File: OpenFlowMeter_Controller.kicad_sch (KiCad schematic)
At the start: 31 parts, among them J3 Conn_01x06, J5 Conn_01x03, J6 Conn_02x04_Odd_Even, J7 Conn_02x03_Odd_Even, U2 STM32F103C8Tx, U5 SN65HVD231, U7 24LC64, Y1 12 MHz

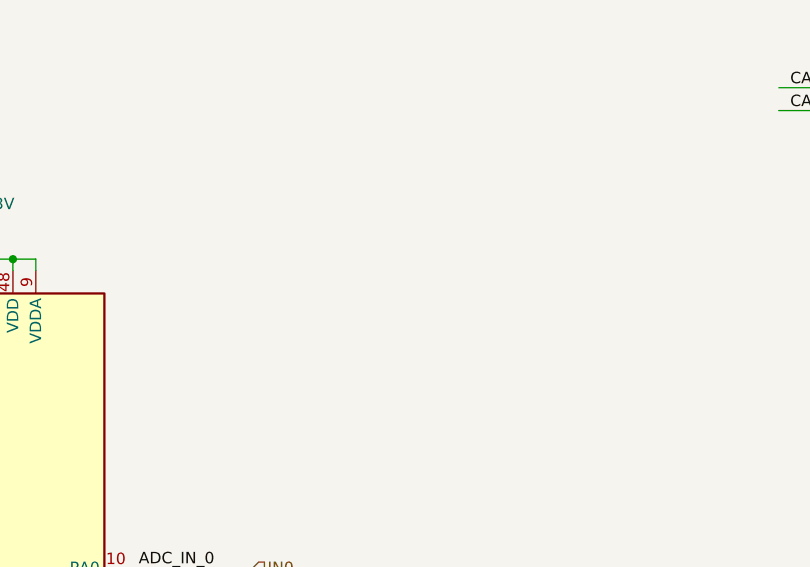
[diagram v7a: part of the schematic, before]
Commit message: added ADC protection
added Zener diodes as ADC input protection in combination with current limiting resistors.
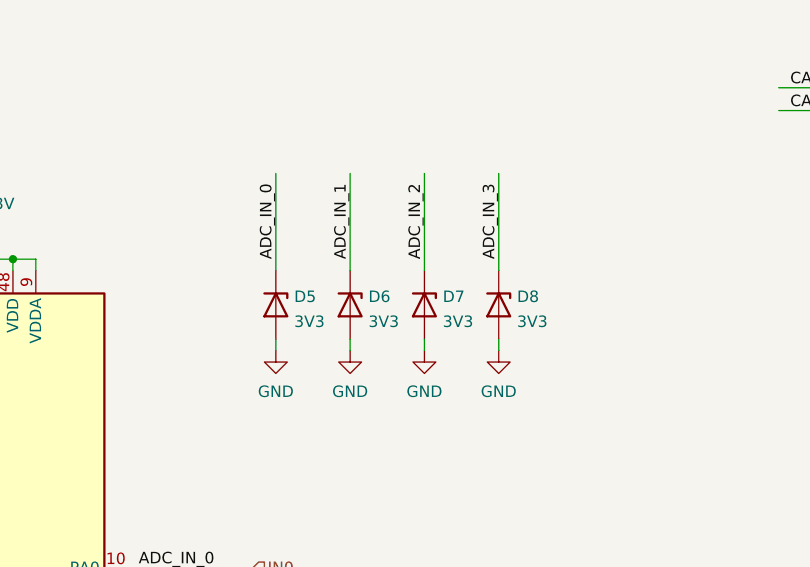
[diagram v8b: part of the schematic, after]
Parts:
- added D5, D6, D7, D8: 3V3, Diode_SMD:D_MiniMELF, symbol Device:D_Zener
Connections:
- net GND: now also D5.2 (A), D6.2 (A), D7.2 (A), D8.2 (A)
- net IN0: now also D5.1 (K)
- net IN1: now also D6.1 (K)
- net IN2: now also D7.1 (K)
- net IN3: now also D8.1 (K)
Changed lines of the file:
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@@
+    (stroke (width 0) (type default) (color 0 0 0 0))
+  )
+  (wire (pts (xy 152.4 50.8) (xy 152.4 40.005))
+    (stroke (width 0) (type default) (color 0 0 0 0))
+  )
+  (wire (pts (xy 160.655 50.8) (xy 160.655 40.005))
     (stroke (width 0) (type default) (color 0 0 0 0))
   )
@@
     (stroke (width 0) (type default) (color 0 0 0 0))
   )
+  (wire (pts (xy 177.165 50.8) (xy 177.165 40.005))
+    (stroke (width 0) (type default) (color 0 0 0 0))
+  )
   (wire (pts (xy 88.9 101.6) (xy 102.87 101.6))
     (stroke (width 0) (type default) (color 0 0 0 0))
@@
     (stroke (width 0) (type default) (color 0 0 0 0))
   )
+  (wire (pts (xy 168.91 58.42) (xy 168.91 59.69))
+    (stroke (width 0) (type default) (color 0 0 0 0))
+  )
   (wire (pts (xy 87.63 53.34) (xy 87.63 55.88))
     (stroke (width 0) (type default) (color 0 0 0 0))
@@
     (stroke (width 0) (type default) (color 0 0 0 0))
   )
+  (wire (pts (xy 152.4 58.42) (xy 152.4 59.69))
+    (stroke (width 0) (type default) (color 0 0 0 0))
+  )
+  (wire (pts (xy 168.91 50.8) (xy 168.91 40.005))
+    (stroke (width 0) (type default) (color 0 0 0 0))
+  )
   (wire (pts (xy 125.73 50.8) (xy 125.73 49.53))
     (stroke (width 0) (type default) (color 0 0 0 0))
@@
     (stroke (width 0) (type default) (color 0 0 0 0))
   )
+  (wire (pts (xy 177.165 58.42) (xy 177.165 59.69))
+    (stroke (width 0) (type default) (color 0 0 0 0))
+  )
   (wire (pts (xy 232.41 66.04) (xy 232.41 67.31))
     (stroke (width 0) (type default) (color 0 0 0 0))
@@
     (stroke (width 0) (type default) (color 0 0 0 0))
   )
+  (wire (pts (xy 160.655 58.42) (xy 160.655 59.69))
+    (stroke (width 0) (type default) (color 0 0 0 0))
+  )
   (wire (pts (xy 88.9 86.36) (xy 102.87 86.36))
     (stroke (width 0) (type default) (color 0 0 0 0))
@@
     (effects (font (size 1.27 1.27)) (justify left bottom))
   )
+  (label "ADC_IN_3" (at 177.165 49.53 90)
+    (effects (font (size 1.27 1.27)) (justify left bottom))
+  )
   (label "SPI_SCK" (at 27.94 163.195 0)
     (effects (font (size 1.27 1.27)) (justify left bottom))
@@
     (effects (font (size 1.27 1.27)) (justify left bottom))
   )
+  (label "ADC_IN_0" (at 152.4 49.53 90)
+    (effects (font (size 1.27 1.27)) (justify left bottom))
+  )
   (label "SPI_MISO" (at 52.07 160.655 0)
     (effects (font (size 1.27 1.27)) (justify left bottom))
@@
     (effects (font (size 1.27 1.27)) (justify left bottom))
   )
+  (label "ADC_IN_1" (at 160.655 49.53 90)
+    (effects (font (size 1.27 1.27)) (justify left bottom))
+  )
   (label "I2C1_SCL" (at 90.17 99.06 0)
     (effects (font (size 1.27 1.27)) (justify left bottom))
@@
   )
   (label "ADC_IN_3" (at 137.16 91.44 0)
+    (effects (font (size 1.27 1.27)) (justify left bottom))
+  )
+  (label "ADC_IN_2" (at 168.91 49.53 90)
     (effects (font (size 1.27 1.27)) (justify left bottom))
   )
@@
     )
     (property "Datasheet" "~" (id 3) (at 96.52 168.91 0)
+      (effects (font (size 1.27 1.27)) hide)
+    )
+    (pin "1")
+    (pin "2")
+  )
+  (symbol (lib_id "Device:D_Zener") (at 177.165 54.61 270) (unit 1)
+    (in_bom yes) (on_board yes) (fields_autoplaced)
+    (property "Reference" "D8" (id 0) (at 179.197 53.7015 90)
+      (effects (font (size 1.27 1.27)) (justify left))
+    )
+    (property "Value" "3V3" (id 1) (at 179.197 56.4766 90)
+      (effects (font (size 1.27 1.27)) (justify left))
+    )
+    (property "Footprint" "Diode_SMD:D_MiniMELF" (id 2) (at 177.165 54.61 0)
+      (effects (font (size 1.27 1.27)) hide)
+    )
+    (property "Datasheet" "~" (id 3) (at 177.165 54.61 0)
       (effects (font (size 1.27 1.27)) hide)
     )
@@
     )
     (property "Datasheet" "" (id 3) (at 29.21 45.72 0)
+      (effects (font (size 1.27 1.27)) hide)
+    )
+    (pin "1")
+  )
+  (symbol (lib_id "power:GND") (at 177.165 59.69 0) (unit 1)
+    (in_bom yes) (on_board yes) (fields_autoplaced)
+    (property "Reference" "#PWR068" (id 0) (at 177.165 66.04 0)
+      (effects (font (size 1.27 1.27)) hide)
+    )
+    (property "Value" "GND" (id 1) (at 177.165 64.2525 0))
+    (property "Footprint" "" (id 2) (at 177.165 59.69 0)
+      (effects (font (size 1.27 1.27)) hide)
+    )
+    (property "Datasheet" "" (id 3) (at 177.165 59.69 0)
       (effects (font (size 1.27 1.27)) hide)
     )
@@
     (pin "8")
   )
+  (symbol (lib_id "power:GND") (at 168.91 59.69 0) (unit 1)
+    (in_bom yes) (on_board yes) (fields_autoplaced)
+    (property "Reference" "#PWR067" (id 0) (at 168.91 66.04 0)
+      (effects (font (size 1.27 1.27)) hide)
+    )
+    (property "Value" "GND" (id 1) (at 168.91 64.2525 0))
+    (property "Footprint" "" (id 2) (at 168.91 59.69 0)
+      (effects (font (size 1.27 1.27)) hide)
+    )
+    (property "Datasheet" "" (id 3) (at 168.91 59.69 0)
+      (effects (font (size 1.27 1.27)) hide)
+    )
+    (pin "1")
+  )
   (symbol (lib_id "Interface_CAN_LIN:SN65HVD231") (at 232.41 33.02 0) (unit 1)
     (in_bom yes) (on_board yes) (fields_autoplaced)
@@
     (pin "1")
   )
+  (symbol (lib_id "power:GND") (at 160.655 59.69 0) (unit 1)
+    (in_bom yes) (on_board yes) (fields_autoplaced)
+    (property "Reference" "#PWR066" (id 0) (at 160.655 66.04 0)
+      (effects (font (size 1.27 1.27)) hide)
+    )
+    (property "Value" "GND" (id 1) (at 160.655 64.2525 0))
+    (property "Footprint" "" (id 2) (at 160.655 59.69 0)
+      (effects (font (size 1.27 1.27)) hide)
+    )
+    (property "Datasheet" "" (id 3) (at 160.655 59.69 0)
+      (effects (font (size 1.27 1.27)) hide)
+    )
+    (pin "1")
+  )
   (symbol (lib_id "Connector_Generic:Conn_02x04_Odd_Even") (at 43.18 179.07 0) (unit 1)
     (in_bom yes) (on_board yes) (fields_autoplaced)
@@
     (pin "8")
   )
+  (symbol (lib_id "Device:D_Zener") (at 160.655 54.61 270) (unit 1)
+    (in_bom yes) (on_board yes) (fields_autoplaced)
+    (property "Reference" "D6" (id 0) (at 162.687 53.7015 90)
+      (effects (font (size 1.27 1.27)) (justify left))
+    )
+    (property "Value" "3V3" (id 1) (at 162.687 56.4766 90)
+      (effects (font (size 1.27 1.27)) (justify left))
+    )
+    (property "Footprint" "Diode_SMD:D_MiniMELF" (id 2) (at 160.655 54.61 0)
+      (effects (font (size 1.27 1.27)) hide)
+    )
+    (property "Datasheet" "~" (id 3) (at 160.655 54.61 0)
+      (effects (font (size 1.27 1.27)) hide)
+    )
+    (pin "1")
+    (pin "2")
+  )
   (symbol (lib_id "power:+3.3V") (at 36.83 175.26 0) (unit 1)
     (in_bom yes) (on_board yes) (fields_autoplaced)
@@
     (pin "2")
   )
+  (symbol (lib_id "Device:D_Zener") (at 168.91 54.61 270) (unit 1)
+    (in_bom yes) (on_board yes) (fields_autoplaced)
+    (property "Reference" "D7" (id 0) (at 170.942 53.7015 90)
+      (effects (font (size 1.27 1.27)) (justify left))
+    )
+    (property "Value" "3V3" (id 1) (at 170.942 56.4766 90)
+      (effects (font (size 1.27 1.27)) (justify left))
+    )
+    (property "Footprint" "Diode_SMD:D_MiniMELF" (id 2) (at 168.91 54.61 0)
+      (effects (font (size 1.27 1.27)) hide)
+    )
+    (property "Datasheet" "~" (id 3) (at 168.91 54.61 0)
+      (effects (font (size 1.27 1.27)) hide)
+    )
+    (pin "1")
+    (pin "2")
+  )
   (symbol (lib_id "Device:C") (at 59.69 35.56 0) (unit 1)
     (in_bom yes) (on_board yes)
@@
     (pin "1")
   )
+  (symbol (lib_id "power:GND") (at 152.4 59.69 0) (unit 1)
+    (in_bom yes) (on_board yes) (fields_autoplaced)
+    (property "Reference" "#PWR065" (id 0) (at 152.4 66.04 0)
+      (effects (font (size 1.27 1.27)) hide)
+    )
+    (property "Value" "GND" (id 1) (at 152.4 64.2525 0))
+    (property "Footprint" "" (id 2) (at 152.4 59.69 0)
+      (effects (font (size 1.27 1.27)) hide)
+    )
+    (property "Datasheet" "" (id 3) (at 152.4 59.69 0)
+      (effects (font (size 1.27 1.27)) hide)
+    )
+    (pin "1")
+  )
   (symbol (lib_id "Device:R") (at 134.62 158.75 0) (unit 1)
     (in_bom yes) (on_board yes) (fields_autoplaced)
@@
     (pin "1")
   )
+  (symbol (lib_id "Device:D_Zener") (at 152.4 54.61 270) (unit 1)
+    (in_bom yes) (on_board yes) (fields_autoplaced)
+    (property "Reference" "D5" (id 0) (at 154.432 53.7015 90)
+      (effects (font (size 1.27 1.27)) (justify left))
+    )
+    (property "Value" "3V3" (id 1) (at 154.432 56.4766 90)
+      (effects (font (size 1.27 1.27)) (justify left))
+    )
+    (property "Footprint" "Diode_SMD:D_MiniMELF" (id 2) (at 152.4 54.61 0)
+      (effects (font (size 1.27 1.27)) hide)
+    )
+    (property "Datasheet" "~" (id 3) (at 152.4 54.61 0)
+      (effects (font (size 1.27 1.27)) hide)
+    )
+    (pin "1")
+    (pin "2")
+  )
   (symbol (lib_id "power:+3.3V") (at 87.63 44.45 0) (unit 1)
